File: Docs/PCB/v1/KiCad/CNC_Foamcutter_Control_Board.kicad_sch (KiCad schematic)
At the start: 29 parts, among them J1 24V_In, J10 Conn_02x04_Odd_Even, J11 State_Pins, J12 SD_Header, J13 Drive_Enable_Header, J14 Drive_Enable_Switches, J15 I2C_Breakout_0, J16 I2C_Breakout_1, J17 GPIO, J2 Buck_In_24V, J3 Buck_In_GND, J4 Buck_Out_5V, J5 Buck_Out_GND, J6 Joy_Header, J7 Button_LED_Negatives, J8 Lvl_Shift_LV, J9 Lvl_Shift_HV, Q1 IRF3205, Q2 IRF3205, Q3 IRF3205, U1 Teensy4.1

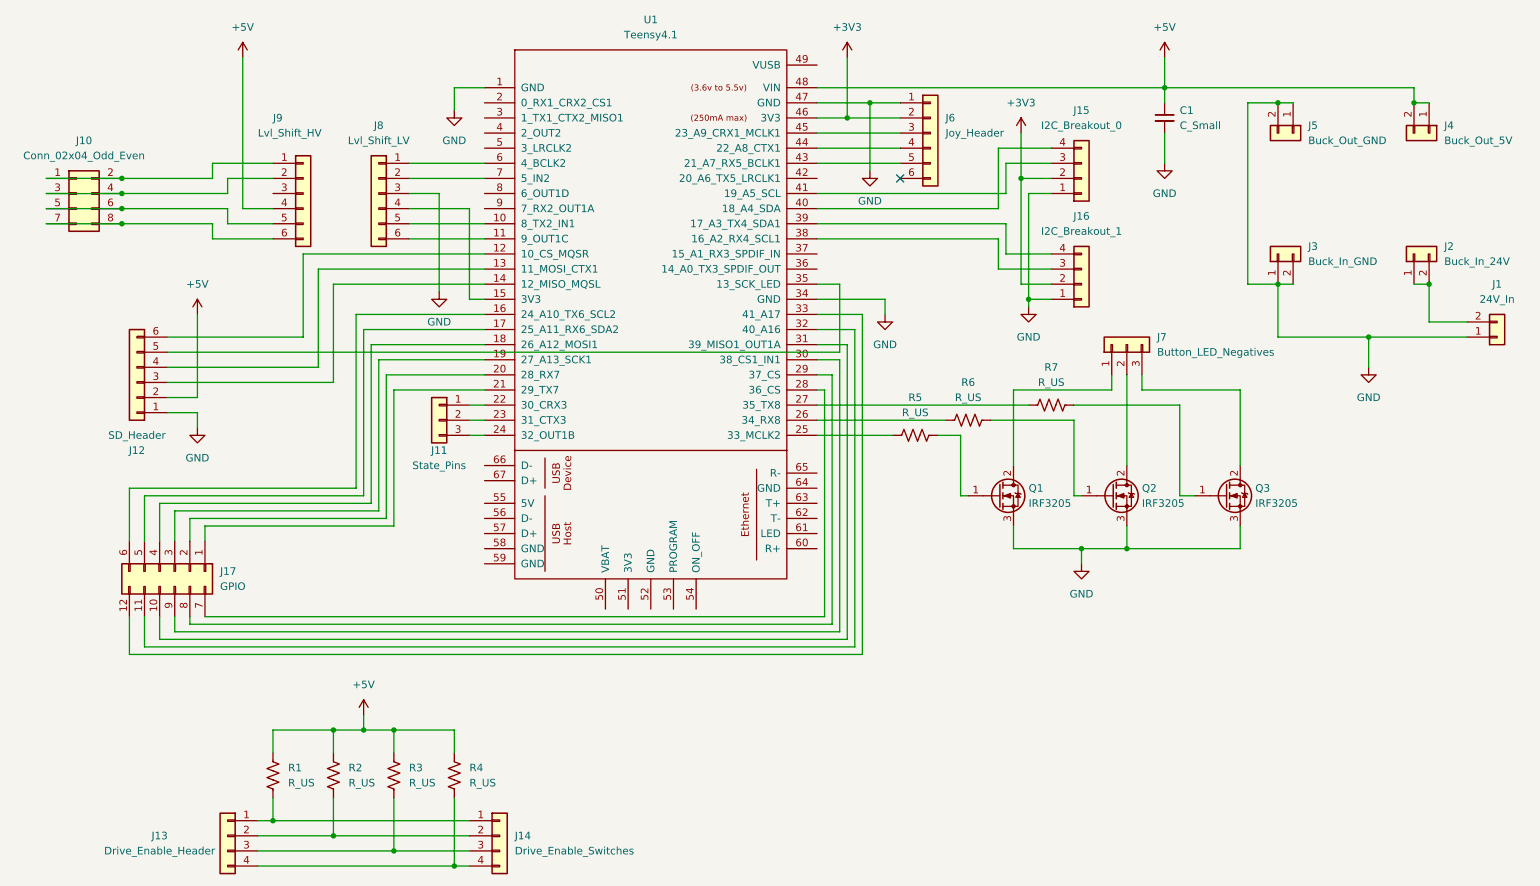
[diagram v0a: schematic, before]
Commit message: Updated Pinout and Schematic for Assembled PCB
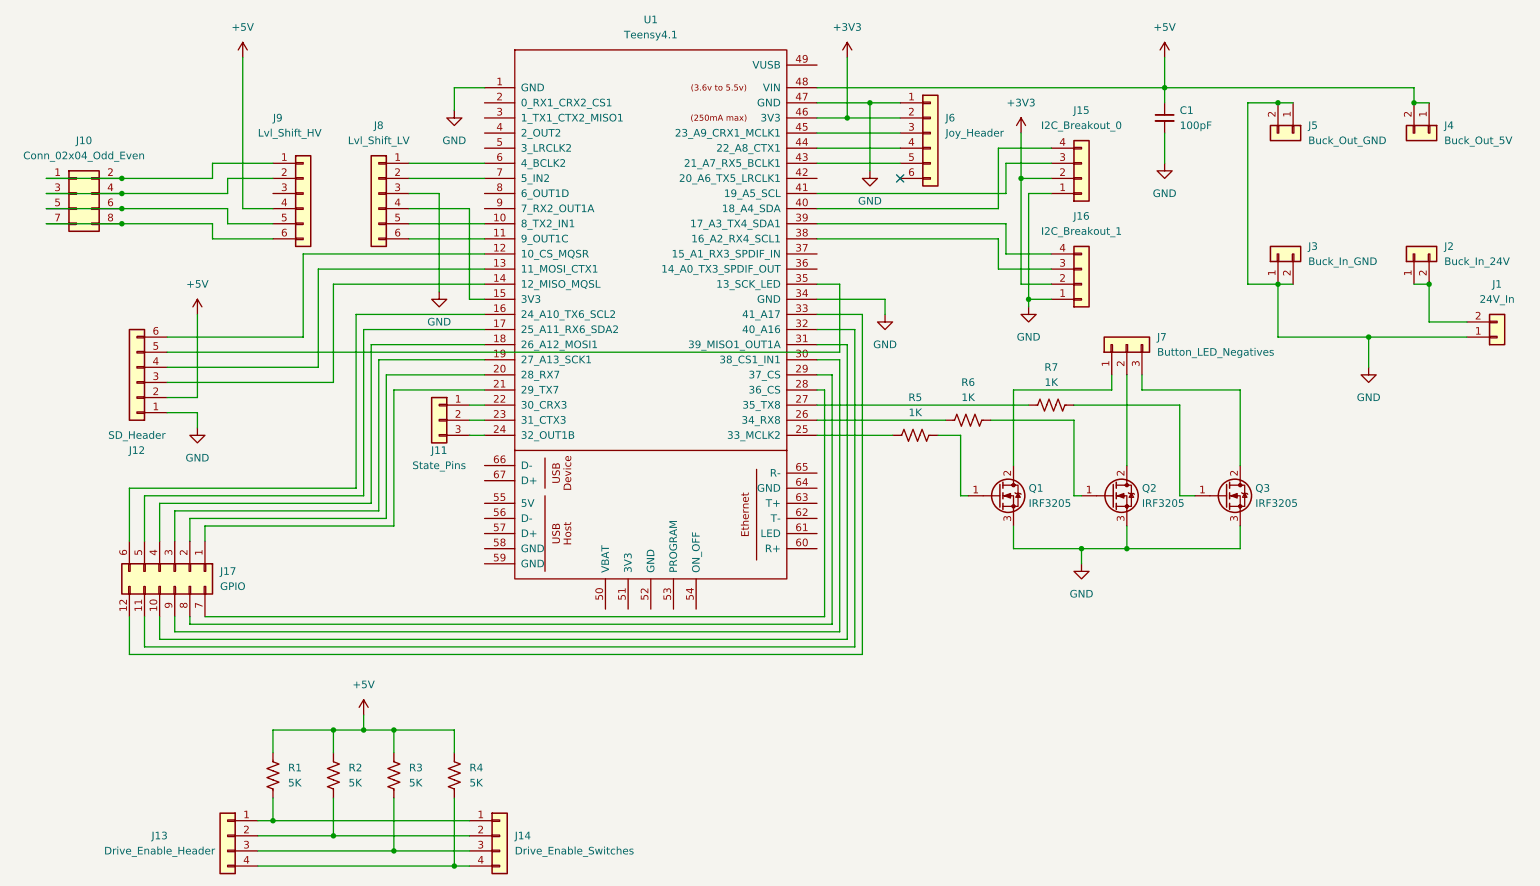
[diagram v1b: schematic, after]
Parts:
- C1: value C_Small -> 100pF
- R1, R2, R3, R4: value R_US -> 5K
- R5, R6, R7: value R_US -> 1K
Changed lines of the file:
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@@
       (effects (font (size 1.27 1.27)) (justify left))
     )
-    (property "Value" "R_US" (id 1) (at 82.55 175.2599 0)
+    (property "Value" "5K" (id 1) (at 82.55 175.2599 0)
       (effects (font (size 1.27 1.27)) (justify left))
     )
@@
     (in_bom yes) (on_board yes) (fields_autoplaced)
     (property "Reference" "R7" (id 0) (at 200.66 105.41 90))
-    (property "Value" "R_US" (id 1) (at 200.66 107.95 90))
+    (property "Value" "1K" (id 1) (at 200.66 107.95 90))
     (property "Footprint" "Resistor_THT:R_Axial_DIN0204_L3.6mm_D1.6mm_P5.08mm_Horizontal" (id 2) (at 200.406 112.776 90)
       (effects (font (size 1.27 1.27)) hide)
@@
     (in_bom yes) (on_board yes) (fields_autoplaced)
     (property "Reference" "R5" (id 0) (at 177.8 110.49 90))
-    (property "Value" "R_US" (id 1) (at 177.8 113.03 90))
+    (property "Value" "1K" (id 1) (at 177.8 113.03 90))
     (property "Footprint" "Resistor_THT:R_Axial_DIN0204_L3.6mm_D1.6mm_P5.08mm_Horizontal" (id 2) (at 178.054 115.824 90)
       (effects (font (size 1.27 1.27)) hide)
@@
     (in_bom yes) (on_board yes) (fields_autoplaced)
     (property "Reference" "R6" (id 0) (at 186.69 107.95 90))
-    (property "Value" "R_US" (id 1) (at 186.69 110.49 90))
+    (property "Value" "1K" (id 1) (at 186.69 110.49 90))
     (property "Footprint" "Resistor_THT:R_Axial_DIN0204_L3.6mm_D1.6mm_P5.08mm_Horizontal" (id 2) (at 186.944 113.284 90)
       (effects (font (size 1.27 1.27)) hide)
@@
       (effects (font (size 1.27 1.27)) (justify left))
     )
-    (property "Value" "C_Small" (id 1) (at 222.25 64.7762 0)
+    (property "Value" "100pF" (id 1) (at 222.25 64.7762 0)
       (effects (font (size 1.27 1.27)) (justify left))
     )
@@
       (effects (font (size 1.27 1.27)) (justify left))
     )
-    (property "Value" "R_US" (id 1) (at 72.39 175.2599 0)
+    (property "Value" "5K" (id 1) (at 72.39 175.2599 0)
       (effects (font (size 1.27 1.27)) (justify left))
     )
@@
       (effects (font (size 1.27 1.27)) (justify left))
     )
-    (property "Value" "R_US" (id 1) (at 92.71 175.2599 0)
+    (property "Value" "5K" (id 1) (at 92.71 175.2599 0)
       (effects (font (size 1.27 1.27)) (justify left))
     )
@@
       (effects (font (size 1.27 1.27)) (justify left))
     )
-    (property "Value" "R_US" (id 1) (at 102.87 175.2599 0)
+    (property "Value" "5K" (id 1) (at 102.87 175.2599 0)
       (effects (font (size 1.27 1.27)) (justify left))
     )
@@
     )
     (path "/73ec39f2-b9c3-4ba6-a3c0-5b587f074196"
-      (reference "C1") (unit 1) (value "C_Small") (footprint "Capacitor_THT:C_Disc_D4.3mm_W1.9mm_P5.00mm")
+      (reference "C1") (unit 1) (value "100pF") (footprint "Capacitor_THT:C_Disc_D4.3mm_W1.9mm_P5.00mm")
     )
     (path "/16d6371a-13f1-4f6f-9a94-302405fdb5f7"
@@
     )
     (path "/8df81e2b-a6c9-43d9-8c16-deb00eac4fe3"
-      (reference "R1") (unit 1) (value "R_US") (footprint "Resistor_THT:R_Axial_DIN0204_L3.6mm_D1.6mm_P5.08mm_Horizontal")
+      (reference "R1") (unit 1) (value "5K") (footprint "Resistor_THT:R_Axial_DIN0204_L3.6mm_D1.6mm_P5.08mm_Horizontal")
     )
     (path "/026b5694-424b-47c2-9250-bea335b34ba0"
-      (reference "R2") (unit 1) (value "R_US") (footprint "Resistor_THT:R_Axial_DIN0204_L3.6mm_D1.6mm_P5.08mm_Horizontal")
+      (reference "R2") (unit 1) (value "5K") (footprint "Resistor_THT:R_Axial_DIN0204_L3.6mm_D1.6mm_P5.08mm_Horizontal")
     )
     (path "/f1123734-62a9-47bd-8372-a603475f7229"
-      (reference "R3") (unit 1) (value "R_US") (footprint "Resistor_THT:R_Axial_DIN0204_L3.6mm_D1.6mm_P5.08mm_Horizontal")
+      (reference "R3") (unit 1) (value "5K") (footprint "Resistor_THT:R_Axial_DIN0204_L3.6mm_D1.6mm_P5.08mm_Horizontal")
     )
     (path "/f4dbd8b7-b9e4-4c5b-99e8-d15cde407d4f"
-      (reference "R4") (unit 1) (value "R_US") (footprint "Resistor_THT:R_Axial_DIN0204_L3.6mm_D1.6mm_P5.08mm_Horizontal")
+      (reference "R4") (unit 1) (value "5K") (footprint "Resistor_THT:R_Axial_DIN0204_L3.6mm_D1.6mm_P5.08mm_Horizontal")
     )
     (path "/18b4b944-4138-46fe-b038-3f70a526ddf2"
-      (reference "R5") (unit 1) (value "R_US") (footprint "Resistor_THT:R_Axial_DIN0204_L3.6mm_D1.6mm_P5.08mm_Horizontal")
+      (reference "R5") (unit 1) (value "1K") (footprint "Resistor_THT:R_Axial_DIN0204_L3.6mm_D1.6mm_P5.08mm_Horizontal")
     )
     (path "/5b397f8d-1ae6-4351-8bb9-79ca84021915"
-      (reference "R6") (unit 1) (value "R_US") (footprint "Resistor_THT:R_Axial_DIN0204_L3.6mm_D1.6mm_P5.08mm_Horizontal")
+      (reference "R6") (unit 1) (value "1K") (footprint "Resistor_THT:R_Axial_DIN0204_L3.6mm_D1.6mm_P5.08mm_Horizontal")
     )
     (path "/11c2a48c-aa11-433f-b168-f76469aa78aa"
-      (reference "R7") (unit 1) (value "R_US") (footprint "Resistor_THT:R_Axial_DIN0204_L3.6mm_D1.6mm_P5.08mm_Horizontal")
+      (reference "R7") (unit 1) (value "1K") (footprint "Resistor_THT:R_Axial_DIN0204_L3.6mm_D1.6mm_P5.08mm_Horizontal")
     )
     (path "/502a96c0-cab7-4e2e-a5ba-b9bf0036312c"
